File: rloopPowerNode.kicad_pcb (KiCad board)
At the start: 2 copper layers, 150 x 200 mm, 112 parts, among them P1 CONN_01X02, P10 CONN_01X03, P11 CONN_01X03, P13 CONN_01X03, P14 CONN_01X03, P15 CONN_01X01, P16 CONN_01X01, P17 CONN_01X08, P18 CONN_01X02, P19 CONN_01X02, P2 CONN_01X02, P20 CONN_01X02, P21 CONN_01X02, P22 AMPMODU-02X05, P23 SHUNT, P3 CONN_01X02, P4 CONN_01X02, P5 CONN_01X01, P6 CONN_01X04, P7 CONN_01X02, P8 CONN_01X02, P9 CONN_01X02, Q1 PMOS, Q2 NMOS, Q3 BSS84, Q4 NMOS, Q5 NMOS, Q6 NMOS, Q7 NMOS, U1 CPC1718, U10 AMC1100, U2 CPC1718, U3 H11F1SM, U4 MAX6814, U5 CPC1718, U6 CPC1718, U7 DS2482-100, U8 MS5607-02BA03, U9 78L05

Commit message: wip some layout, added a diode to watchdog power
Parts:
- added D20: D_Schottky, Diodes_SMD:SOD-123, F.Cu at (40.5, 214.0)
- added REF**: PCBOUTLINE-POWERNODE, -footprints:PCBOUTLINE-POWERNODE, F.Cu at (35.0, 35.0)
- F1: footprint Fuse_Holders_and_Fuses:BladeFuse-CarType -> Fuse_Holders_and_Fuses:Fuseholder5x20_horiz_open_universal_Type-III
- R20: footprint Resistors_SMD:R_1206 -> Resistors_SMD:R_0603
- moved P8 349.3 mm to (-69.5, 95.0), turned to 270 degrees
- moved D5 340.8 mm to (-62.5, 93.0), turned to 0 degrees
- moved D18 335.4 mm to (91.0, 81.5), turned to 270 degrees
- moved R9 333.7 mm to (-60.5, 103.0), turned to 180 degrees
- moved Q7 333.3 mm to (83.0, 83.0), turned to 180 degrees
- moved R35 331.8 mm to (89.0, 81.5), turned to 90 degrees
- moved U5 328.4 mm to (-52.5, 92.0), turned to 90 degrees
- moved R6 327.3 mm to (-48.5, 84.0), turned to 0 degrees
- moved R34 324.2 mm to (83.0, 89.0), turned to 90 degrees
- moved R37 317.6 mm to (94.0, 84.5), turned to 180 degrees
- moved R36 315.3 mm to (94.0, 86.5), turned to 180 degrees
- moved D19 309.8 mm to (82.0, 96.0), turned to 90 degrees
- moved P13 302.8 mm to (65.5, 351.5), turned to 180 degrees
- moved Q2 302.7 mm to (58.5, 218.5), turned to 180 degrees
- moved R1 298.1 mm to (44.5, 208.5), turned to 180 degrees
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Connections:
- JP3 pad 1: Net-(JP3-Pad1) -> Net-(D20-Pad1)
- Q2 pad 4: Net-(JP3-Pad1) -> Net-(D20-Pad1)
- R1 pad 2: Net-(JP3-Pad1) -> Net-(D20-Pad2)
- R10 pad 1: Net-(R10-Pad1) -> BATT-ILV
- R10 pad 2: BATT-ILV -> Net-(R10-Pad2)
- R2 pad 2: Net-(JP3-Pad1) -> Net-(D20-Pad2)
- RL1 pad 4: DCDC-POS -> DCDC-NEG
- RL1 pad 5: BATT-POS -> BATT-NEG
- RL1 pad 7: DCDC-NEG -> DCDC-POS
- RL1 pad 8: BATT-NEG -> BATT-POS
- U1 pad 1: BATT-POS -> BATT-NEG
- U1 pad 2: DCDC-POS -> DCDC-NEG
- U2 pad 1: DCDC-NEG -> DCDC-POS
- U2 pad 2: BATT-NEG -> BATT-POS
- U3 pad 6: Net-(JP3-Pad1) -> Net-(D20-Pad2)
- U6 pad 1: Net-(R10-Pad1) -> Net-(R10-Pad2)
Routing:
- net BATT-NEG: track 0.00 -> 68.6 mm
- net DCDC-POS: track 0.00 -> 64.7 mm
- net DCDC-NEG: track 0.00 -> 47.0 mm, vias 0 -> 2
- net BATT-POS: track 0.00 -> 23.0 mm
- net Net-(D20-Pad1): track 0.00 -> 21.0 mm, vias 0 -> 1
- net ILV+: track 0.00 -> 19.8 mm, vias 0 -> 1
- net GND: track 0.00 -> 15.7 mm, vias 0 -> 2
- net BATT-ILV: track 0.00 -> 14.3 mm
- net +5V-HV: track 0.00 -> 10.6 mm
- net Net-(R38-Pad2): track 0.00 -> 9.80 mm
- net Net-(R38-Pad1): track 0.00 -> 9.64 mm
- net Net-(R3-Pad2): track 0.00 -> 9.47 mm
- net Net-(D20-Pad2): track 0.00 -> 9.26 mm
- net Net-(R10-Pad2): track 0.00 -> 8.53 mm
- net Net-(D2-Pad1): track 0.00 -> 7.48 mm
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- added copper zone on F.Cu, net BATT-NEG
- added copper zone on B.Cu, net BATT-POS
- added copper zone on B.Cu, net DCDC-NEG
- added copper zone on F.Cu, net DCDC-NEG
- added copper zone on In1.Cu(GND), net DCDC-NEG
- added copper zone on B.Cu, net DCDC-POS
- added copper zone on B.Cu, net Net-(F1-Pad2)
- added copper zone on B.Cu, net Net-(F2-Pad2)
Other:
- copper layers 2 -> 4
- net class Default: trace_width 0.25 -> 0.3; via_dia 0.6 -> 0.8; via_drill 0.4 -> 0.5
- net class GLV added: clearance 0.4, trace_width 0.3, via_dia 0.8, via_drill 0.5
- net class IHV added: clearance 0.9, trace_width 2, via_dia 0.8, via_drill 0.5
- net class ILV added: clearance 0.4, trace_width 0.3, via_dia 0.8, via_drill 0.5
- rule via_min_size: 0.4 -> 0.5

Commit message: wip layout, most subcircuits
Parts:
- moved C2 285.1 mm to (237.5, 111.5)
- moved Q3 285.1 mm to (230.5, 114.5)
- moved U7 285.1 mm to (237.5, 116.5)
- moved P10 263.8 mm to (226.5, 131.5)
- moved P11 263.8 mm to (226.5, 120.5)
- moved P13 263.8 mm to (226.5, 142.5)
- moved P14 263.8 mm to (226.5, 109.5)
- moved P4 255.8 mm to (43.0, 174.0), turned to 90 degrees
- moved D17 250.2 mm to (47.0, 174.0), turned to 270 degrees
- moved R30 246.0 mm to (50.0, 174.0), turned to 90 degrees
- moved P3 241.0 mm to (43.0, 185.0), turned to 90 degrees
- moved Q6 239.8 mm to (54.0, 175.0), turned to 90 degrees
- moved D16 239.6 mm to (54.0, 169.0), turned to 180 degrees
- moved R31 239.0 mm to (54.0, 172.0), turned to 0 degrees
- moved D15 235.6 mm to (47.0, 185.0), turned to 270 degrees
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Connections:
- P6 pad M1: (no net) -> BATT-NEG
- P6 pad M2: (no net) -> BATT-NEG
- P7 pad M1: (no net) -> GND
- P7 pad M2: (no net) -> GND
- P8 pad M1: (no net) -> BATT-NEG
- P8 pad M2: (no net) -> BATT-NEG
- P9 pad M1: (no net) -> BATT-NEG
- P9 pad M2: (no net) -> BATT-NEG
- R9 pad 1: Net-(R9-Pad1) -> BATT-POS
- R9 pad 2: BATT-POS -> Net-(R9-Pad2)
- U5 pad 1: Net-(R9-Pad1) -> Net-(R9-Pad2)
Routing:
- net Net-(U2-Pad3): track 0.00 -> 205.7 mm, vias 0 -> 2
- net RELAY-COMMON: track 0.00 -> 165.7 mm, vias 0 -> 4
- net +24V: track 0.00 -> 135.6 mm, vias 0 -> 1
- net Net-(D1-Pad1): track 0.13 -> 100.9 mm, vias 0 -> 2
- net Net-(U1-Pad3): track 0.00 -> 56.9 mm
- net BATT-NEG: track 68.6 -> 25.5 mm
- net GND: track 15.7 -> 53.7 mm
- net BATT-POS: track 23.0 -> 58.4 mm
- net DCDC-POS: track 64.7 -> 92.6 mm
- net /Relay Driver 4/RELAY-NEG: track 0.00 -> 12.6 mm
- net Net-(D5-Pad2): track 0.00 -> 8.18 mm
- net Net-(Q7-Pad3): track 0.00 -> 8.08 mm
- net /Relay Driver 3/RELAY-NEG: track 0.00 -> 7.39 mm
- net /Relay Driver 2/RELAY-NEG: track 0.00 -> 7.33 mm
- net /Relay Driver 1/RELAY-NEG: track 0.00 -> 7.33 mm
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- added copper zone on F.Cu, net +24V
- added copper zone on B.Cu, net BATT-NEG
- added copper zone on B.Cu, net GND
- added copper zone on F.Cu, net GND
- added copper zone on In1.Cu(GND), net GND
- added copper zone on F.Cu, net GNDA

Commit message: wip, bigger pads on relays, placed sensors
HV current sensor flipped polarity
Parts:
- removed REF**: PCBOUTLINE-POWERNODE, -footprints:PCBOUTLINE-POWERNODE
- added C11: 100n, Capacitors_SMD:C_0603, F.Cu at (99.0, 220.5)
- added JP4: Jumper_NC_Small, -footprints:SOLDERJUMPER, F.Cu at (51.0, 146.0)
- added JP5: Jumper_NC_Small, -footprints:SOLDERJUMPER, F.Cu at (87.0, 211.8)
- added JP6: Jumper_NC_Small, -footprints:SOLDERJUMPER, F.Cu at (92.0, 229.0)
- added PCB1: PCB-OUTLINE, -footprints:PCBOUTLINE-POWERNODE, F.Cu at (35.6, 35.2)
- added R39: 10, Resistors_SMD:R_0603, F.Cu at (100.5, 223.0)
- added R40: 10, Resistors_SMD:R_0603, F.Cu at (97.5, 223.0)
- C8, C9: footprint Capacitors_SMD:C_0603 -> Capacitors_SMD:C_1206
- moved U8 195.4 mm to (82.0, 56.0)
- moved C4 195.2 mm to (78.5, 55.4)
- moved P13 189.0 mm to (64.0, 46.0), turned to 90 degrees
- moved P10 174.0 mm to (75.0, 46.0), turned to 90 degrees
- moved P11 159.0 mm to (86.0, 46.0), turned to 90 degrees
- moved U7 158.7 mm to (90.2, 57.2), turned to 270 degrees
- moved Q3 153.3 mm to (91.0, 51.0), turned to 90 degrees
- moved C2 152.8 mm to (94.7, 57.2), turned to 90 degrees
- moved P14 144.2 mm to (97.0, 46.0), turned to 90 degrees
- moved R20 8.56 mm to (99.0, 198.5)
- moved C10 8.54 mm to (100.0, 196.0), turned to 0 degrees
- moved U10 6.50 mm to (99.0, 209.5)
- moved C8 6.26 mm to (99.0, 201.5), turned to 0 degrees
- moved C9 5.70 mm to (99.0, 218.0), turned to 180 degrees
- moved D18 3.50 mm to (88.0, 104.0)
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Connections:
- C5 pad 2: DCDC-NEG -> DCDC-NEG-2
- C6 pad 2: DCDC-NEG -> DCDC-NEG-2
- C7 pad 2: DCDC-NEG -> DCDC-NEG-2
- C9 pad 1: DCDC-NEG -> DCDC-NEG-2
- P21 pad 1: DCDC-NEG -> DCDC-NEG-2
- P23 pad 1: DCDC-NEG -> Net-(JP6-Pad1)
- U10 pad 2: Net-(P23-Pad2) -> Net-(C11-Pad2)
- U10 pad 3: DCDC-NEG -> Net-(C11-Pad1)
- U10 pad 4: DCDC-NEG -> DCDC-NEG-2
- U10 pad 6: GNDA -> Net-(R20-Pad2)
- U10 pad 7: Net-(R20-Pad2) -> GNDA
- U9 pad GND: DCDC-NEG -> DCDC-NEG-2
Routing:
- net +3V3: track 0.00 -> 74.7 mm, vias 0 -> 3
- net Net-(P10-Pad3): track 0.00 -> 47.8 mm
- net Net-(U1-Pad3): track 56.9 -> 98.3 mm, vias 0 -> 2
- net GND: track 53.7 -> 75.2 mm
- net Net-(Q3-Pad1): track 0.00 -> 13.8 mm, vias 0 -> 2
- net GNDA: track 0.00 -> 12.6 mm, vias 0 -> 2
- net SENS-SDA: track 0.00 -> 12.1 mm, vias 0 -> 1
- net /Relay Driver 4/RELAY-NEG: track 12.6 -> 3.36 mm
- net +24V: track 135.6 -> 126.5 mm, vias 1 -> 2
- net Net-(JP6-Pad1): track 0.00 -> 9.04 mm
- net Net-(C11-Pad1): track 0.00 -> 8.74 mm
- net Net-(C11-Pad2): track 0.00 -> 8.53 mm
- net BATT-NEG: track 25.5 -> 33.1 mm
- net SENS-SCL: track 0.00 -> 7.05 mm, vias 0 -> 1
- net Net-(U2-Pad3): track 205.7 -> 211.7 mm
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- added copper zone on F.Cu, net /Relay Driver 4/RELAY-NEG
- added copper zone on F.Cu, net DCDC-NEG-2
- removed copper zone on F.Cu, net DCDC-NEG
- removed copper zone on In1.Cu(GND), net DCDC-NEG
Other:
- net class IHV-GND-2 added: clearance 1.5, trace_width 0.3, via_dia 0.8, via_drill 0.5

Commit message: added backup hookups/testpoints, a lot more routing
subcircuits are essentially complete except the BMS mount and the node
core, the hookups are a backup in case the node core doesn't get
finished
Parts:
- added A1: NODE_CORE_CONNECTOR, -footprints:NODE-CORE, F.Cu at (170.0, 209.0)
- added P12: CONN_01X02, Pin_Headers:Pin_Header_Straight_1x02, F.Cu at (61.0, 197.0)
- added P24: CONN_01X02, Pin_Headers:Pin_Header_Straight_1x02, F.Cu at (61.0, 186.0)
- added P25: CONN_01X02, Pin_Headers:Pin_Header_Straight_1x02, F.Cu at (61.0, 178.0)
- added P26: CONN_01X02, Pin_Headers:Pin_Header_Straight_1x02, F.Cu at (82.0, 79.0)
- added P27: CONN_01X02, Pin_Headers:Pin_Header_Straight_1x02, F.Cu at (38.0, 203.0)
- added P28: CONN_01X02, Pin_Headers:Pin_Header_Straight_1x02, F.Cu at (46.0, 203.0)
- added P29: CONN_02X02, Pin_Headers:Pin_Header_Straight_2x02, F.Cu at (93.0, 196.0)
- added P30: CONN_02X02, Pin_Headers:Pin_Header_Straight_2x02, F.Cu at (107.0, 193.0)
- added P31: CONN_01X02, Pin_Headers:Pin_Header_Straight_1x02, F.Cu at (70.0, 65.0)
- added P32: CONN_01X02, Pin_Headers:Pin_Header_Straight_1x02, F.Cu at (70.0, 74.0)
- added P33: CONN_01X02, Pin_Headers:Pin_Header_Straight_1x02, F.Cu at (88.0, 65.0)
- added P34: CONN_01X02, Pin_Headers:Pin_Header_Straight_1x02, F.Cu at (83.0, 65.0)
- added P35: CONN_02X02, Pin_Headers:Pin_Header_Straight_2x02, F.Cu at (55.5, 161.5)
- added P36: CONN_01X02, Pin_Headers:Pin_Header_Straight_1x02, F.Cu at (78.0, 65.0)
- added P37: CONN_02X02, Pin_Headers:Pin_Header_Straight_2x02, F.Cu at (94.5, 204.0)
- added REF**: BMS-PCB-OUTLINE, -footprints:BMS-PCB-OUTLINE, F.Cu at (115.0, 47.5)
- JP4, JP5: footprint -footprints:SOLDERJUMPER -> Resistors_SMD:R_1206_HandSoldering
- moved C3 302.9 mm to (103.5, 201.5), turned to 270 degrees
- moved D4 302.9 mm to (109.5, 201.5), turned to 270 degrees
- moved R11 302.9 mm to (106.5, 201.5), turned to 270 degrees
- moved R8 296.9 mm to (103.5, 195.0), turned to 270 degrees
- moved D11 202.2 mm to (131.4, 123.7)
- moved P22 202.2 mm to (139.1, 117.5)
- moved R17 202.2 mm to (144.4, 117.2)
- moved R18 202.2 mm to (144.4, 113.9)
- moved R19 202.2 mm to (133.9, 124.7)
- moved R21 202.2 mm to (135.9, 124.7)
- moved R7 6.40 mm to (67.0, 74.0), turned to 90 degrees
- moved JP5 6.05 mm to (81.0, 211.0)
- moved JP4 1.00 mm to (52.0, 146.0)
- moved PCB1 0.63 mm to (35.0, 35.0)
- moved D1 0.50 mm to (64.0, 222.0)
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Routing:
- net +24V: track 126.5 -> 206.0 mm, vias 2 -> 6
- net Net-(JP4-Pad2): track 0.00 -> 74.2 mm, vias 0 -> 2
- net GLV: track 0.00 -> 16.6 mm
- net +3V3: track 74.7 -> 90.8 mm, vias 3 -> 4
- net SENS-SCL: track 7.05 -> 21.7 mm
- net +5V: track 2.27 -> 15.2 mm, vias 0 -> 1
- net DCDC-POS: track 91.8 -> 104.1 mm
- net BATT-POS: track 58.9 -> 71.2 mm
- net +3.3V: track 0.00 -> 10.1 mm
- net RLY-DCDC: track 4.00 -> 13.8 mm
- net BATT-NEG: track 33.1 -> 42.0 mm
- net DCDC-NEG-2: track 2.65 -> 9.10 mm, vias 0 -> 2
- net HV-CURR: track 1.88 -> 8.13 mm
- net SENS-SDA: track 12.1 -> 18.3 mm
- net WDT: track 0.00 -> 6.06 mm
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- added copper zone on B.Cu, net DCDC-NEG-2
- added copper zone on In1.Cu(GND), net DCDC-NEG-2
- added copper zone on B.Cu, net GNDA
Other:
- net class Default: via_dia 0.8 -> 0.85
- net class GLV: via_dia 0.8 -> 0.85
- net class IHV: via_dia 0.8 -> 0.85
- net class IHV-GND-2: via_dia 0.8 -> 0.85
- net class ILV: via_dia 0.8 -> 0.85

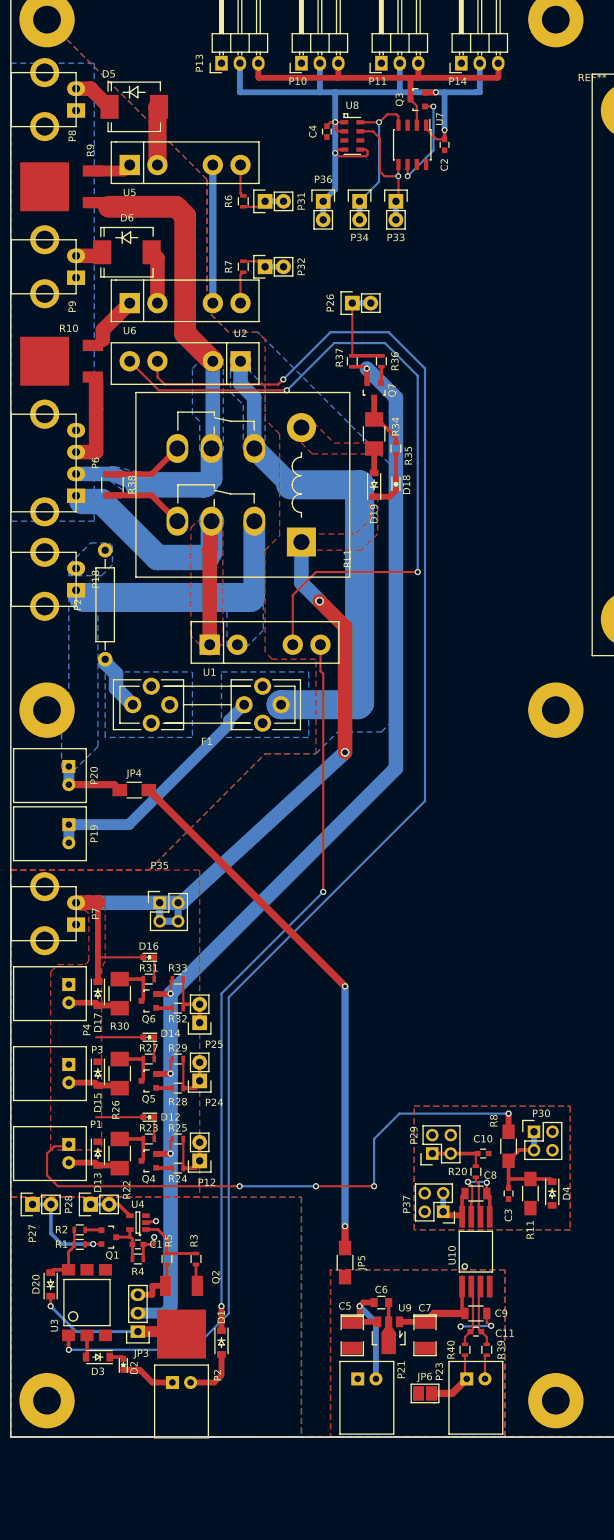
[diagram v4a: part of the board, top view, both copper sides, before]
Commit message: added diode for 78L05, moved some stuff, more routing
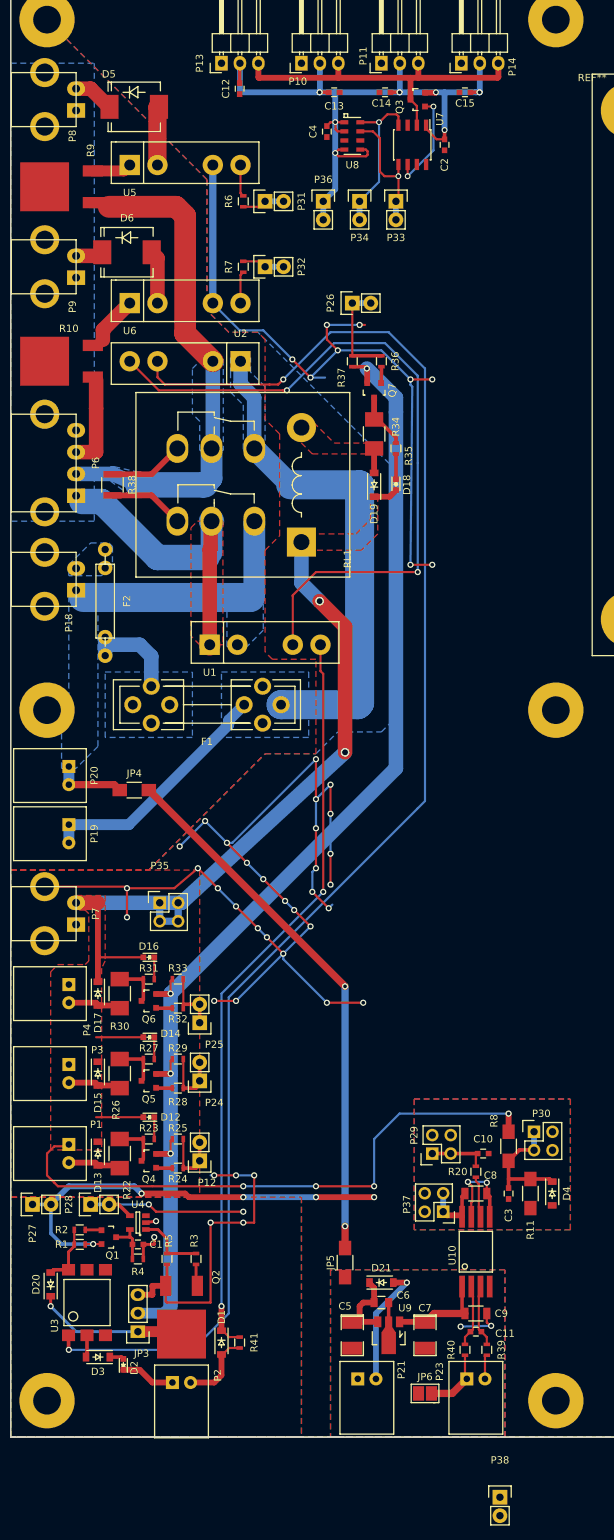
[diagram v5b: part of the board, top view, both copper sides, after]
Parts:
- added C12: 1u, Capacitors_SMD:C_0603, F.Cu at (66.5, 49.5)
- added C13: 1u, Capacitors_SMD:C_0603, F.Cu at (79.5, 50.0)
- added C14: 1u, Capacitors_SMD:C_0603, F.Cu at (86.5, 50.0)
- added C15: 1u, Capacitors_SMD:C_0603, F.Cu at (97.5, 50.0)
- added D21: D, Diodes_SMD:SOD-123, F.Cu at (86.0, 213.8)
- added P38: CONN_01X02, Pin_Headers:Pin_Header_Straight_1x02, F.Cu at (102.3, 243.3)
- added R41: ?, Resistors_SMD:R_0603, F.Cu at (66.5, 222.0)
- F2: footprint Resistors_ThroughHole:Resistor_Horizontal_RM15mm -> -footprints:FUSE-MULTICHOICE
- moved F2 0.50 mm to (48.0, 127.5)
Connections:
- C5 pad 1: ILV+ -> Net-(C5-Pad1)
- C6 pad 1: ILV+ -> Net-(C5-Pad1)
- U9 pad VI: ILV+ -> Net-(C5-Pad1)
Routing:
- net GND: track 78.7 -> 350.4 mm, vias 2 -> 46
- net +5V: track 15.2 -> 61.4 mm, vias 1 -> 5
- net WDT: track 6.06 -> 24.9 mm, vias 0 -> 2
- net Net-(C5-Pad1): track 0.00 -> 11.8 mm
- net +3V3: track 90.8 -> 97.4 mm, vias 4 -> 7
- net Net-(F1-Pad2): track 7.85 -> 13.7 mm
- net Net-(D1-Pad2): track 7.53 -> 10.4 mm
- net Net-(D1-Pad1): track 100.3 -> 103.2 mm
- net ILV+: track 19.8 -> 16.9 mm

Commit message: reordered all reference designators
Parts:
- removed the D10 at (369.0, 98.0)
- removed the D7 at (388.0, 97.0)
- removed the D8 at (358.0, 99.0)
- removed the D9 at (374.0, 91.0)
- removed the P15 at (258.0, 82.0)
- removed the P16 at (269.0, 76.0)
- removed the P17 at (374.0, 111.0)
- removed the R12 at (391.1, 83.8)
- removed the R13 at (394.9, 126.9)
- removed the R14 at (343.7, 78.7)
- removed the R15 at (374.0, 100.0)
- removed the R16 at (386.5, 75.4)
- moved JP2 162.2 mm to (124.9, 156.7)
- moved JP1 151.8 mm to (133.6, 146.0)
- renumbered C6 to C10, C7 to C11, C8 to C12, C9 to C13, C11 to C14, C10 to C15, C12 to C4, C13 to C5, C14 to C6, C15 to C7, C4 to C8, C5 to C9, D12 to D10, D13 to D11, D14 to D12, D15 to D13, D16 to D14, D17 to D15, D18 to D16, D19 to D17, D20 to D2, D2 to D3, D3 to D4, D4 to D5, D5 to D6, D6 to D7, D21 to D8, D11 to D9, JP6 to JP4, JP4 to JP5, JP5 to JP6, P9 to P10, P13 to P11, P14 to P12, P18 to P13, P19 to P14, P20 to P15, P21 to P16, P22 to P17, P23 to P18, P12 to P19, P24 to P20, P25 to P21, P26 to P22, P27 to P23, P28 to P24, P29 to P25, P30 to P26, P31 to P27, P32 to P28, P33 to P29, P34 to P30, P35 to P31, P36 to P32, P37 to P33, P38 to P34, P6 to P5, P7 to P6, P10 to P7, P11 to P8, P8 to P9, R41 to R1, R8 to R10, R9 to R11, R10 to R12, R11 to R13, R17 to R14, R18 to R15, R19 to R16, R39 to R17, R21 to R18, R20 to R19, R38 to R2, R40 to R20, R22 to R21, R23 to R22, R24 to R23, R25 to R24, R26 to R25, R27 to R26, R28 to R27, R29 to R28, R30 to R29, R1 to R3, R31 to R30, R32 to R31, R33 to R32, R34 to R33, R35 to R34, R36 to R35, R37 to R36, R2 to R4, R3 to R5, R4 to R6, R5 to R7, R6 to R8, R7 to R9
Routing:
- net GND: track 350.4 -> 363.4 mm, vias 46 -> 45
